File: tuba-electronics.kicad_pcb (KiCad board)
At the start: 2 copper layers, 128.1 x 128.1 mm, 23 parts, among them J10 Conn_01x06, J11 Conn_01x04, J7 Conn_01x05, J8 Conn_01x10, J9 Conn_01x05

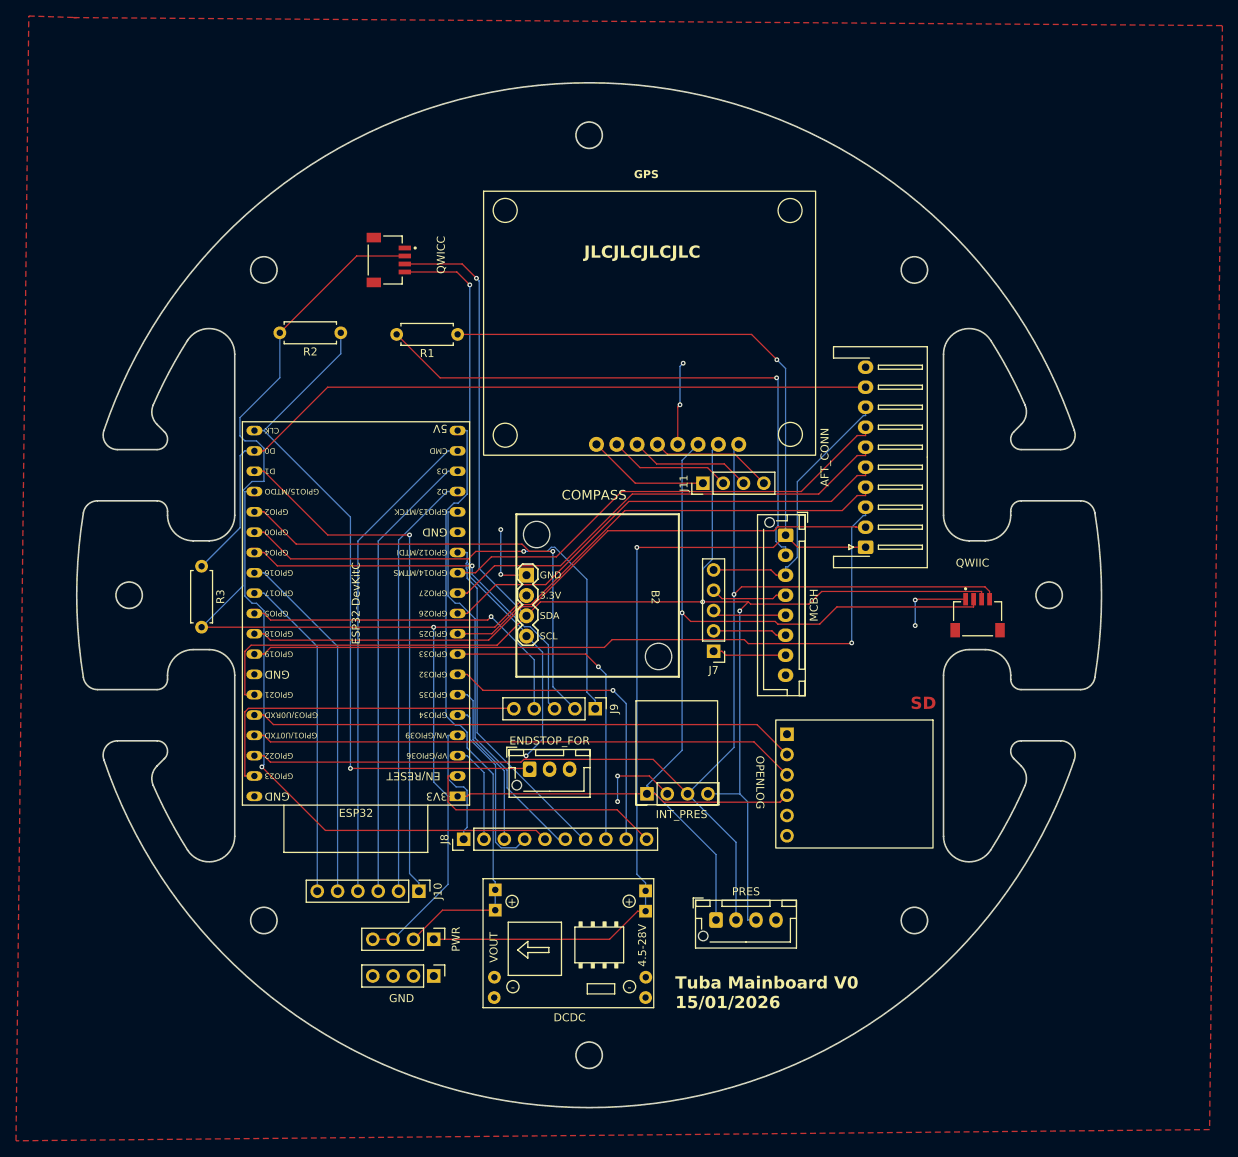
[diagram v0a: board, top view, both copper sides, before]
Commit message: changed limit switches GPIOs, added pics
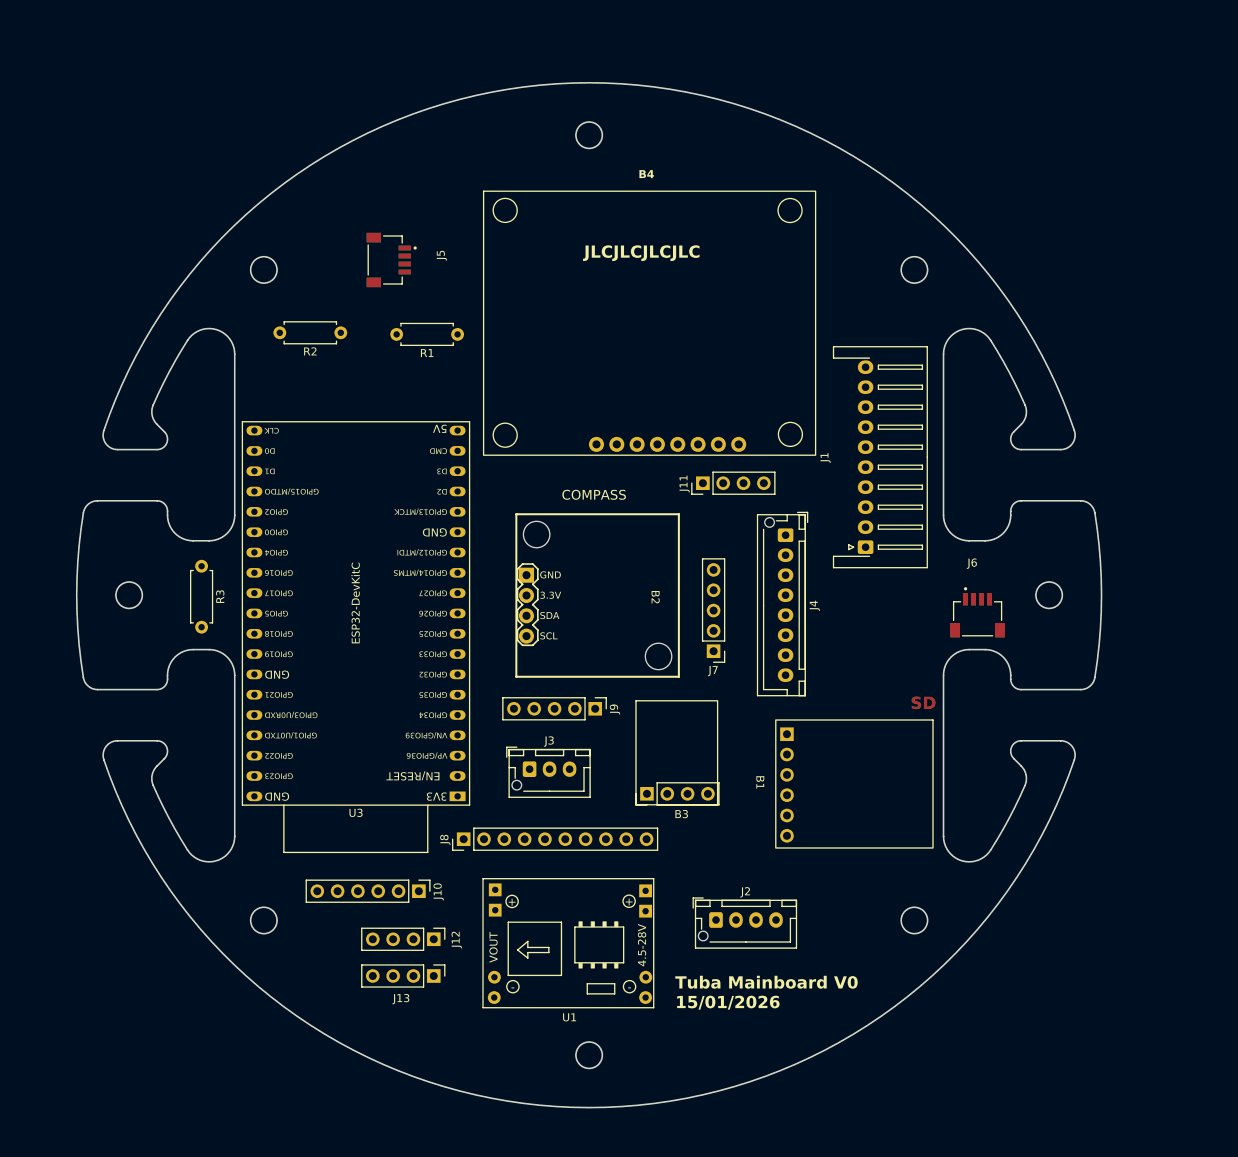
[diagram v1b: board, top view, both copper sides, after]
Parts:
- J1: renamed from AFT_CONN; value Conn_01x08 -> Conn_01x10
- renumbered OPENLOG to B1, INT_PRES to B3, GPS to B4, PWR to J12, GND to J13, PRES to J2, ENDSTOP_FOR to J3, MCBH to J4, QWICC to J5, QWIIC to J6, DCDC to U1, ESP32 to U3
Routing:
- net +3V3: track 300.9 -> 0.00 mm, vias 2 -> 0
- net /I2C_SCL: track 227.4 -> 0.00 mm, vias 3 -> 0
- net /I2C_SDA: track 223.6 -> 0.00 mm, vias 3 -> 0
- net VCC: track 167.3 -> 0.00 mm, vias 2 -> 0
- net /ENDSTOP_AFT: track 97.5 -> 0.00 mm
- net /IN2_P: track 93.5 -> 0.00 mm, vias 1 -> 0
- net /ENDSTOP_FOR: track 86.5 -> 0.00 mm, vias 1 -> 0
- net /IN1_P: track 82.6 -> 0.00 mm
- net +5V: track 77.2 -> 0.00 mm
- net Net-(J8-Pin_5): track 76.2 -> 0.00 mm, vias 1 -> 0
- net /SWITCH_1: track 72.9 -> 0.00 mm, vias 1 -> 0
- net /TX0: track 68.6 -> 0.00 mm
- net /RX0: track 68.6 -> 0.00 mm
- net Net-(J10-Pin_1): track 67.7 -> 0.00 mm, vias 1 -> 0
- net Net-(J9-Pin_1): track 61.8 -> 0.00 mm, vias 1 -> 0
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- removed copper zone on F.Cu, net GND
